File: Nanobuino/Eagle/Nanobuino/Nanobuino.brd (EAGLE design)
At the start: 70.1 x 70.1 mm, 2 parts, among them J1 HEAD15-NOSS, J2 HEAD15-NOSS-1

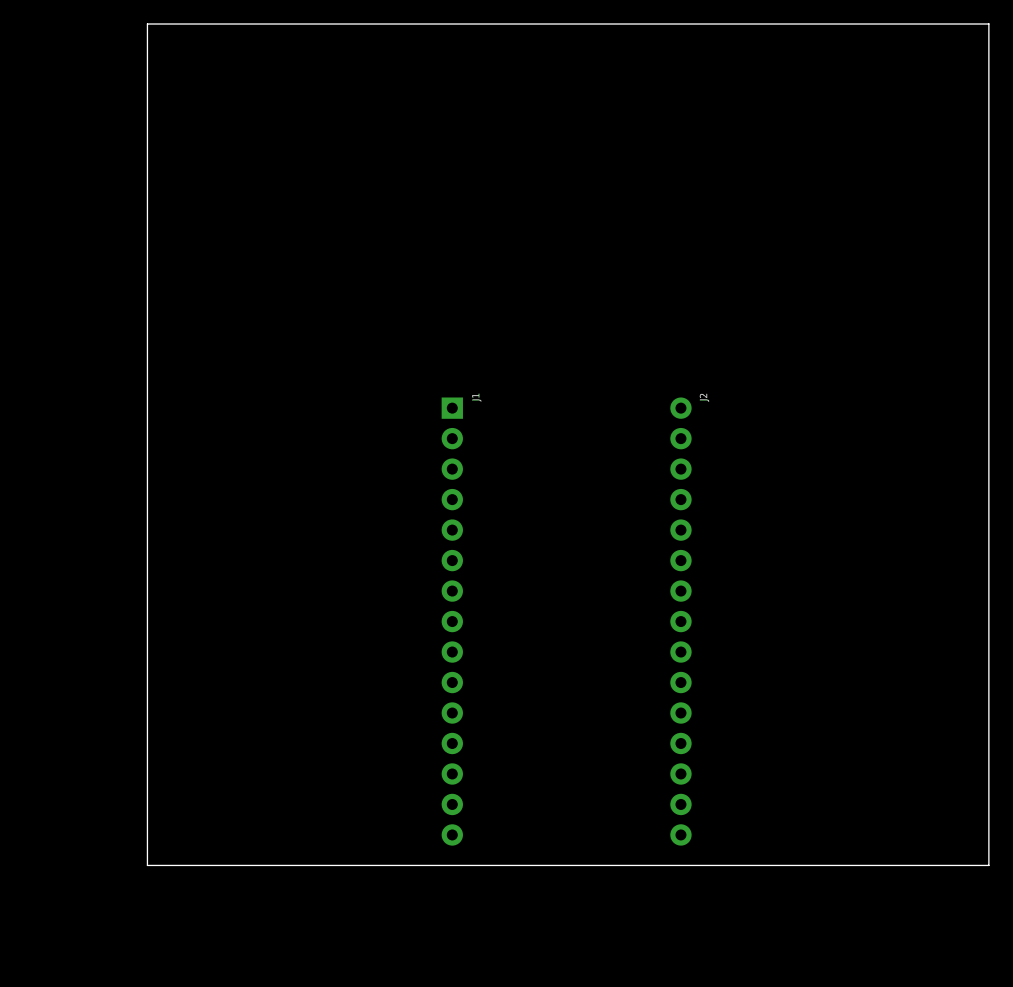
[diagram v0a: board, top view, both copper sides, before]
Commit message: Lots of parts added to schematic
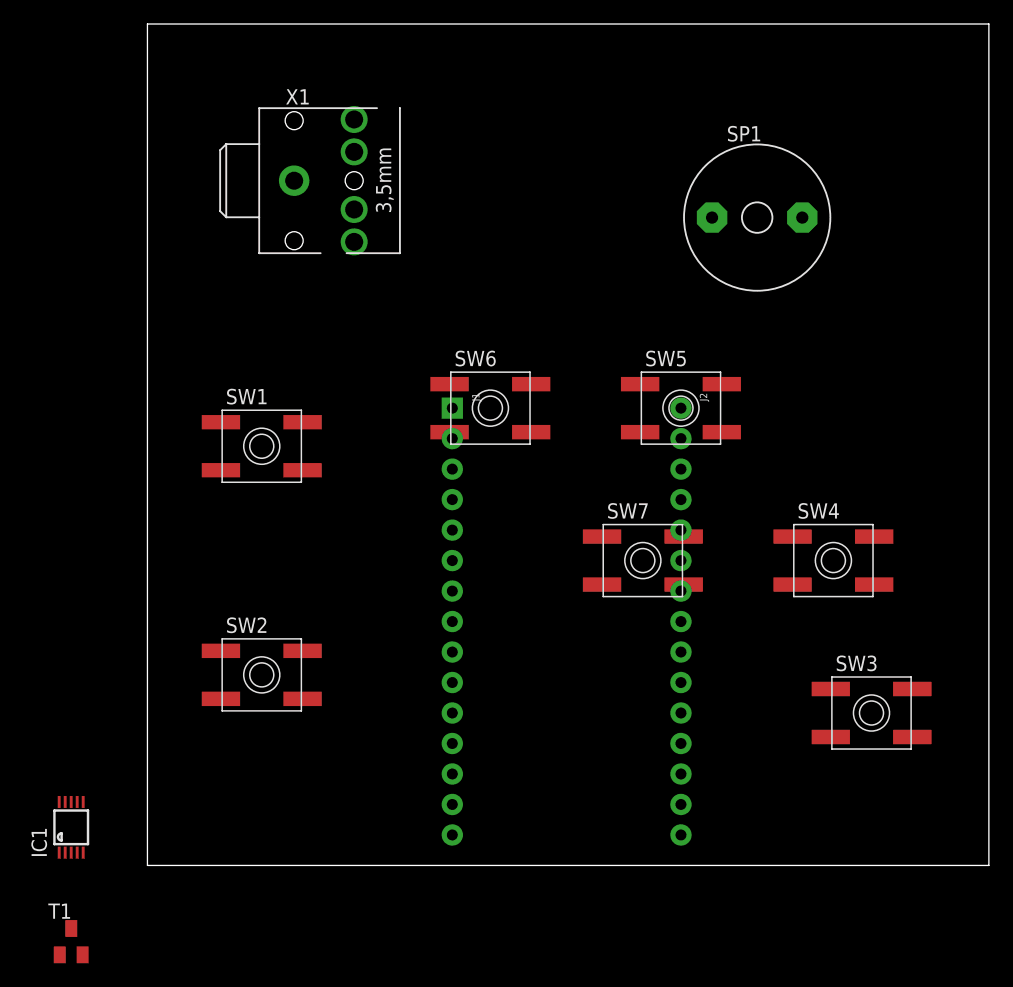
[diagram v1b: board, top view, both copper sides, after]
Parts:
- added IC1: MCP73833-UN, adafruit:MSOP10
- added SP1: SPEAKER/AL60P, adafruit:AL60P
- added SW1, SW2, SW3, SW4, SW5, SW6, SW7: SPST_TACT-EVQQ2, adafruit:EVQ-Q2
- added T1: (no value), transistor-neu-to92:SOT23-BEC
- added X1: STEREOJACK, adafruit:STX3100
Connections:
- new net GND: IC1.5
- new net VDD1: IC1.1
- new net VDD2: IC1.2
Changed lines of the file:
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@@
 <layer number="54" name="bGND_GNDA" color="1" fill="9" visible="no" active="no"/>
 <layer number="56" name="wert" color="7" fill="1" visible="no" active="no"/>
+<layer number="57" name="tCAD" color="7" fill="1" visible="no" active="no"/>
 <layer number="91" name="Nets" color="2" fill="1" visible="no" active="no"/>
 <layer number="92" name="Busses" color="1" fill="1" visible="no" active="no"/>
@@
 <layer number="101" name="Patch_Top" color="12" fill="4" visible="yes" active="yes"/>
 <layer number="102" name="Vscore" color="7" fill="1" visible="yes" active="yes"/>
+<layer number="103" name="fp3" color="7" fill="1" visible="no" active="yes"/>
 <layer number="104" name="Name" color="7" fill="1" visible="yes" active="yes"/>
+<layer number="105" name="Beschreib" color="9" fill="1" visible="yes" active="yes"/>
+<layer number="106" name="BGA-Top" color="4" fill="1" visible="yes" active="yes"/>
+<layer number="107" name="BD-Top" color="5" fill="1" visible="yes" active="yes"/>
+<layer number="108" name="fp8" color="7" fill="1" visible="no" active="yes"/>
+<layer number="109" name="fp9" color="7" fill="1" visible="no" active="yes"/>
+<layer number="110" name="fp0" color="7" fill="1" visible="no" active="yes"/>
+<layer number="111" name="LPC17xx" color="7" fill="1" visible="yes" active="yes"/>
+<layer number="112" name="tSilk" color="7" fill="1" visible="yes" active="yes"/>
 <layer number="116" name="Patch_BOT" color="9" fill="4" visible="yes" active="yes"/>
 <layer number="121" name="_tsilk" color="7" fill="1" visible="yes" active="yes"/>
 <layer number="122" name="_bsilk" color="7" fill="1" visible="yes" active="yes"/>
+<layer number="123" name="tTestmark" color="7" fill="1" visible="no" active="yes"/>
+<layer number="124" name="bTestmark" color="7" fill="1" visible="no" active="yes"/>
+<layer number="125" name="_tNames" color="7" fill="1" visible="yes" active="yes"/>
+<layer number="126" name="_bNames" color="7" fill="1" visible="yes" active="yes"/>
+<layer number="127" name="_tValues" color="7" fill="1" visible="yes" active="yes"/>
+<layer number="128" name="_bValues" color="7" fill="1" visible="yes" active="yes"/>
+<layer number="131" name="tAdjust" color="7" fill="1" visible="no" active="yes"/>
+<layer number="132" name="bAdjust" color="7" fill="1" visible="no" active="yes"/>
+<layer number="144" name="Drill_legend" color="7" fill="1" visible="yes" active="yes"/>
+<layer number="150" name="Notes" color="7" fill="1" visible="no" active="yes"/>
 <layer number="151" name="HeatSink" color="7" fill="1" visible="yes" active="yes"/>
+<layer number="152" name="_bDocu" color="7" fill="1" visible="yes" active="yes"/>
+<layer number="153" name="FabDoc1" color="6" fill="1" visible="no" active="no"/>
+<layer number="154" name="FabDoc2" color="2" fill="1" visible="no" active="no"/>
+<layer number="155" name="FabDoc3" color="7" fill="15" visible="no" active="no"/>
+<layer number="199" name="Contour" color="7" fill="1" visible="yes" active="yes"/>
 <layer number="200" name="200bmp" color="1" fill="10" visible="no" active="no"/>
 <layer number="201" name="201bmp" color="2" fill="1" visible="no" active="no"/>
 <layer number="202" name="202bmp" color="3" fill="1" visible="no" active="no"/>
+<layer number="203" name="203bmp" color="4" fill="10" visible="yes" active="yes"/>
+<layer number="204" name="204bmp" color="5" fill="10" visible="yes" active="yes"/>
+<layer number="205" name="205bmp" color="6" fill="10" visible="yes" active="yes"/>
+<layer number="206" name="206bmp" color="7" fill="10" visible="yes" active="yes"/>
+<layer number="207" name="207bmp" color="8" fill="10" visible="yes" active="yes"/>
+<layer number="208" name="208bmp" color="9" fill="10" visible="yes" active="yes"/>
+<layer number="209" name="209bmp" color="7" fill="1" visible="no" active="yes"/>
+<layer number="210" name="210bmp" color="7" fill="1" visible="no" active="yes"/>
+<layer number="211" name="211bmp" color="7" fill="1" visible="yes" active="yes"/>
+<layer number="212" name="212bmp" color="7" fill="1" visible="yes" active="yes"/>
+<layer number="213" name="213bmp" color="7" fill="1" visible="yes" active="yes"/>
+<layer number="214" name="214bmp" color="7" fill="1" visible="yes" active="yes"/>
+<layer number="215" name="215bmp" color="7" fill="1" visible="yes" active="yes"/>
+<layer number="216" name="216bmp" color="7" fill="1" visible="yes" active="yes"/>
+<layer number="217" name="217bmp" color="18" fill="1" visible="no" active="no"/>
+<layer number="218" name="218bmp" color="19" fill="1" visible="no" active="no"/>
+<layer number="219" name="219bmp" color="20" fill="1" visible="no" active="no"/>
+<layer number="220" name="220bmp" color="21" fill="1" visible="no" active="no"/>
+<layer number="221" name="221bmp" color="22" fill="1" visible="no" active="no"/>
+<layer number="222" name="222bmp" color="23" fill="1" visible="no" active="no"/>
+<layer number="223" name="223bmp" color="24" fill="1" visible="no" active="no"/>
+<layer number="224" name="224bmp" color="25" fill="1" visible="no" active="no"/>
+<layer number="248" name="Housing" color="7" fill="1" visible="yes" active="yes"/>
+<layer number="249" name="Edge" color="7" fill="1" visible="yes" active="yes"/>
 <layer number="250" name="Descript" color="3" fill="1" visible="no" active="no"/>
 <layer number="251" name="SMDround" color="12" fill="11" visible="no" active="no"/>
@@
 <element name="J1" library="MyCON2" package="HEAD15-NOSS" value="HEAD15-NOSS" x="25.4" y="38.1" rot="R270"/>
 <element name="J2" library="MyCON2" package="HEAD15-NOSS-1" value="HEAD15-NOSS-1" x="44.45" y="38.1" rot="R270"/>
+<element name="X1" library="adafruit" package="STX3100" value="STEREOJACK" x="9.525" y="57.15"/>
+<element name="SP1" library="adafruit" package="AL60P" value="SPEAKER/AL60P" x="50.8" y="53.975"/>
+<element name="SW1" library="adafruit" package="EVQ-Q2" value="SPST_TACT-EVQQ2" x="9.525" y="34.925"/>
+<element name="SW2" library="adafruit" package="EVQ-Q2" value="SPST_TACT-EVQQ2" x="9.525" y="15.875"/>
+<element name="SW3" library="adafruit" package="EVQ-Q2" value="SPST_TACT-EVQQ2" x="60.325" y="12.7"/>
+<element name="SW4" library="adafruit" package="EVQ-Q2" value="SPST_TACT-EVQQ2" x="57.15" y="25.4"/>
+<element name="SW5" library="adafruit" package="EVQ-Q2" value="SPST_TACT-EVQQ2" x="44.45" y="38.1"/>
+<element name="SW6" library="adafruit" package="EVQ-Q2" value="SPST_TACT-EVQQ2" x="28.575" y="38.1"/>
+<element name="SW7" library="adafruit" package="EVQ-Q2" value="SPST_TACT-EVQQ2" x="41.275" y="25.4"/>
+<element name="IC1" library="adafruit" package="MSOP10" value="MCP73833-UN" x="-6.35" y="3.175"/>
+<element name="T1" library="transistor-neu-to92" package="SOT23-BEC" value="" x="-6.35" y="-6.35"/>
 </elements>
 <signals>
@@
 <contactref element="J1" pad="2"/>
 </signal>
+<signal name="VDD1">
+<contactref element="IC1" pad="1"/>
+</signal>
+<signal name="VDD2">
+<contactref element="IC1" pad="2"/>
+</signal>
+<signal name="GND">
+<contactref element="IC1" pad="5"/>
+</signal>
 </signals>
